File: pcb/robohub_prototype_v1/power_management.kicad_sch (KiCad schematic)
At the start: 134 parts, among them J21 Barrel_Jack_Switch_Pin3Ring, U21 LM3880, U22 TPS564242DRL, U23 TPS564242DRL, U24 TPS564242DRL, U25 TPS564242DRL, U26 TPS564242DRL, U27 TPS564242DRL

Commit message: Update paths to footprint libraries. Begin adding footprints for PDN resistors. Create master BOM
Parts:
- R211, R216, R217, R220, R224, R27, R28: footprint (none) -> Resistor_SMD:R_0402_1005Metric
- U22, U23, U24, U25, U26, U27: footprint custom_footprint:TPS564247DRLR -> fryelabs:TPS564247DRLR
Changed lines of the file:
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@@
 			)
 		)
-		(property "Footprint" "custom_footprint:TPS564247DRLR"
+		(property "Footprint" "fryelabs:TPS564247DRLR"
 			(at 165.1 134.62 0)
 			(effects
@@
 			)
 		)
-		(property "Footprint" "custom_footprint:TPS564247DRLR"
+		(property "Footprint" "fryelabs:TPS564247DRLR"
 			(at 163.83 257.81 0)
 			(effects
@@
 			)
 		)
-		(property "Footprint" ""
+		(property "Footprint" "Resistor_SMD:R_0402_1005Metric"
 			(at 130.302 262.89 90)
 			(effects
@@
 			)
 		)
-		(property "Footprint" "custom_footprint:TPS564247DRLR"
+		(property "Footprint" "fryelabs:TPS564247DRLR"
 			(at 162.56 381 0)
 			(effects
@@
 			)
 		)
-		(property "Footprint" ""
+		(property "Footprint" "Resistor_SMD:R_0402_1005Metric"
 			(at 130.302 325.12 90)
 			(effects
@@
 			)
 		)
-		(property "Footprint" ""
+		(property "Footprint" "Resistor_SMD:R_0402_1005Metric"
 			(at 187.452 320.04 90)
 			(effects
@@
 			)
 		)
-		(property "Footprint" ""
+		(property "Footprint" "Resistor_SMD:R_0402_1005Metric"
 			(at 129.032 445.77 90)
 			(effects
@@
 			)
 		)
-		(property "Footprint" ""
+		(property "Footprint" "Resistor_SMD:R_0402_1005Metric"
 			(at 187.452 198.12 90)
 			(effects
@@
 			)
 		)
-		(property "Footprint" ""
+		(property "Footprint" "Resistor_SMD:R_0402_1005Metric"
 			(at 129.032 386.08 90)
 			(effects
@@
 			)
 		)
-		(property "Footprint" "custom_footprint:TPS564247DRLR"
+		(property "Footprint" "fryelabs:TPS564247DRLR"
 			(at 163.83 198.12 0)
 			(effects
@@
 			)
 		)
-		(property "Footprint" ""
+		(property "Footprint" "Resistor_SMD:R_0402_1005Metric"
 			(at 130.302 203.2 90)
 			(effects
@@
 			)
 		)
-		(property "Footprint" "custom_footprint:TPS564247DRLR"
+		(property "Footprint" "fryelabs:TPS564247DRLR"
 			(at 162.56 440.69 0)
 			(effects
@@
 			)
 		)
-		(property "Footprint" "custom_footprint:TPS564247DRLR"
+		(property "Footprint" "fryelabs:TPS564247DRLR"
 			(at 163.83 320.04 0)
 			(effects

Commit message: Begin PDN circuit design/BOM/layout
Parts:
- removed D21, D22, D23: D_Schottky, symbol Device:D_Schottky
- C210, C217, C218, C228, C229, C29: footprint (none) -> Capacitor_SMD:C_0603_1608Metric
- C214, C215, C216, C226, C227, C26, C2602, C27, C28: footprint (none) -> Capacitor_SMD:C_1206_3216Metric
- L21, L24, L25: value 1u -> 2.2u; footprint (none) -> Inductor_SMD:L_0805_2012Metric
- R21, R210, R215, R219, R223, R26: footprint (none) -> Resistor_SMD:R_0402_1005Metric
- R212, R23: value 135k -> 100k; footprint (none) -> Resistor_SMD:R_0402_1005Metric
- R213, R24, R29: value 30k -> 22.1k; footprint (none) -> Resistor_SMD:R_0402_1005Metric
- R22: footprint (none) -> Resistor_SMD:R_0603_1608Metric
- R28: value 135k -> 100k
- U22, U23, U24, U25, U26, U27: footprint fryelabs:TPS564247DRLR -> fryelabs_kicad_footprint_lib:TPS564247DRLR
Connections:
- net VCC_3_3_A_SW: now reaches L21.1, U22.2 (SW)
- net VCC_3A_EN: now reaches R21.2, R22.1, U22.5 (EN)
- net VCC_3_3_A_FB: now reaches R23.2, R24.1, U22.6 (FB)
- net VCC_3_3_C_SW: now reaches L25.1, U24.2 (SW)
- net VCC_3_3C_EN: now reaches R210.2, R211.1, U24.5 (EN)
- net VCC_3_3_C_FB: now reaches R212.2, R213.1, U24.6 (FB)
- net VCC_3_3_B_FB: now reaches R28.2, R29.1, U23.6 (FB)
- net VCC_3_3B_EN: now reaches R26.2, R27.1, U23.5 (EN)
- net VCC_3_3_B_SW: now reaches L24.1, U23.2 (SW)
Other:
- note added: "- Processor Clock Frequency 500MHz"
- note added: "Key: R1 = R23 R2 = R24"
- note added: "Relevant Info for PDN"
- note added: "V_out = 0.6*(1+(R1/R2))"
- moved on the sheet: C210, C214, C215, C216, C226, C227, C26, C2602, C27, C28, C29, R21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

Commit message: Update paths for footprints top adjacent lib directory at above clone. Finish basic regulator layout/BOM. Link 3d STEPs into model. Rearrangle layout
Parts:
- removed D24, D25, D26: D_Schottky, symbol Device:D_Schottky
- removed R210, R219, R223, R26: 100k, Resistor_SMD:R_0402_1005Metric, symbol Device:R
- removed R211, R220, R224, R27: 36.5k, Resistor_SMD:R_0402_1005Metric, symbol Device:R
- C233, C234, C235, C240, C241, C242, C257, C258, C259: footprint (none) -> Capacitor_SMD:C_1206_3216Metric
- C236, C237, C243, C244, C260, C261: footprint (none) -> Capacitor_SMD:C_0603_1608Metric
- L26, L28, L29: footprint (none) -> Inductor_SMD:L_0805_2012Metric
- R216: footprint Resistor_SMD:R_0402_1005Metric -> Resistor_SMD:R_0603_1608Metric
- R218, R221, R222: footprint (none) -> Resistor_SMD:R_0402_1005Metric
- R225: value 95k -> 32k; footprint (none) -> Resistor_SMD:R_0402_1005Metric
- R226: value 30k -> 10k; footprint (none) -> Resistor_SMD:R_0402_1005Metric
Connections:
- net VCC_3A_EN is gone; now on net PS_GRP1_EN_DIV: R21.2, R22.1, U22.5 (EN)
- net VCC_3_3B_EN is gone; now on net PS_GRP1_EN_DIV: U23.5 (EN)
- net VCC_3_3C_EN is gone; now on net PS_GRP1_EN_DIV: U24.5 (EN)
- net VCC_1_2_DDR_SW: now reaches L28.1, U26.2 (SW)
- net PS_GRP1_EN_DIV: now reaches U26.5 (EN)
- net VCC_1_2_DDR_FB: now reaches R221.2, R222.1, U26.6 (FB)
- net PS_GRP2_EN_DIV: now reaches R215.2, R216.1, U25.5 (EN)
- net PS_GRP2_EN_DIV: now also U27.5 (EN)
- net VCC_1_2_FB: now reaches R217.2, R218.1, U25.6 (FB)
- net VCC_1_2_SW: now reaches L26.1, U25.2 (SW)
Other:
- moved on the sheet: C233, C234, C235, C240, C241, C242, C257, C258, C259, R215, R216, U25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

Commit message: Add fuse to PCB design
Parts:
- added F1: Fuse, fryelabs_kicad_footprint_lib:0ZCF0050FF2C, symbol Device:Fuse
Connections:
- net 5V: now also F1.2; no longer J21.1
- new net VCC: F1.1, J21.1
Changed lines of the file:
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@@
 	)
 	(junction
+		(at 67.31 73.66)
+		(diameter 0)
+		(color 0 0 0 0)
+	)
+	(junction
 		(at 353.06 412.75)
 		(diameter 0)
@@
 	(polyline
 		(pts
-			(xy 83.82 91.44) (xy 83.82 48.26)
+			(xy 105.41 92.71) (xy 105.41 49.53)
 		)
 		(stroke
@@
 		)
 	)
-	(polyline
-		(pts
-			(xy 25.4 48.26) (xy 25.4 50.8)
-		)
-		(stroke
-			(width 0)
-			(type default)
-		)
-	)
 	(wire
 		(pts
@@
 	(wire
 		(pts
+			(xy 67.31 73.66) (xy 72.39 73.66)
+		)
+		(stroke
+			(width 0)
+			(type default)
+		)
+	)
+	(wire
+		(pts
 			(xy 316.23 412.75) (xy 316.23 426.72)
 		)
@@
 	(polyline
 		(pts
-			(xy 25.4 91.44) (xy 83.82 91.44)
+			(xy 25.4 92.71) (xy 105.41 92.71)
 		)
 		(stroke
@@
 	(polyline
 		(pts
-			(xy 25.4 52.07) (xy 25.4 91.44)
+			(xy 25.4 49.53) (xy 25.4 91.44)
 		)
 		(stroke
@@
 	(wire
 		(pts
+			(xy 86.36 67.31) (xy 86.36 73.66)
+		)
+		(stroke
+			(width 0)
+			(type default)
+		)
+	)
+	(wire
+		(pts
 			(xy 111.76 314.96) (xy 111.76 317.5)
 		)
@@
 	(polyline
 		(pts
-			(xy 83.82 48.26) (xy 25.4 48.26)
+			(xy 105.41 49.53) (xy 25.4 49.53)
 		)
 		(stroke
@@
 	(wire
 		(pts
+			(xy 80.01 73.66) (xy 86.36 73.66)
+		)
+		(stroke
+			(width 0)
+			(type default)
+		)
+	)
+	(wire
+		(pts
 			(xy 210.82 199.39) (xy 210.82 193.04)
 		)
@@
 	(global_label "5V"
 		(shape input)
+		(at 86.36 67.31 90)
+		(fields_autoplaced yes)
+		(effects
+			(font
+				(size 1.27 1.27)
+			)
+			(justify left)
+		)
+		(property "Intersheetrefs" "${INTERSHEET_REFS}"
+			(at 86.2806 62.5988 90)
+			(effects
+				(font
+					(size 1.27 1.27)
+				)
+				(justify left)
+				(hide yes)
+			)
+		)
+	)
+	(global_label "VCC"
+		(shape input)
 		(at 67.31 67.31 90)
 		(fields_autoplaced yes)
@@
 		)
 		(property "Intersheetrefs" "${INTERSHEET_REFS}"
-			(at 67.2306 62.5988 90)
+			(at 67.31 60.6962 90)
 			(effects
 				(font
@@
 					(unit 1)
 				)
+			)
+		)
+	)
+	(symbol
+		(lib_id "Device:Fuse")
+		(at 76.2 73.66 90)
+		(unit 1)
+		(exclude_from_sim no)
+		(in_bom yes)
+		(on_board yes)
+		(dnp no)
+		(fields_autoplaced yes)
+		(property "Reference" "F1"
+			(at 76.2 67.31 90)
+			(effects
+				(font
+					(size 1.27 1.27)
+				)
+			)
+		)
+		(property "Value" "Fuse"
+			(at 76.2 69.85 90)
+			(effects
+				(font
+					(size 1.27 1.27)
+				)
+			)
+		)
+		(property "Footprint" "fryelabs_kicad_footprint_lib:0ZCF0050FF2C"
+			(at 76.2 75.438 90)
+			(effects
+				(font
+					(size 1.27 1.27)
+				)
+				(hide yes)
+			)
+		)
+		(property "Datasheet" "~"
+			(at 76.2 73.66 0)
+			(effects
+				(font
+					(size 1.27 1.27)
+				)
+				(hide yes)
+			)
+		)
+		(property "Description" "Fuse"
+			(at 76.2 73.66 0)
+			(effects
+				(font
+					(size 1.27 1.27)
+				)
+				(hide yes)
+			)
+		)
+		(pin "2"
+		)
+		(pin "1"
+		)
+		(instances
+			(project "robohub_prototype_v1"
+				(path "/bc29dce2-fa63-43eb-9ef7-3b495f27cc69/73c1b947-11e9-40cf-af03-56c22766304e"
+					(reference "F1")
+					(unit 1)
+				)

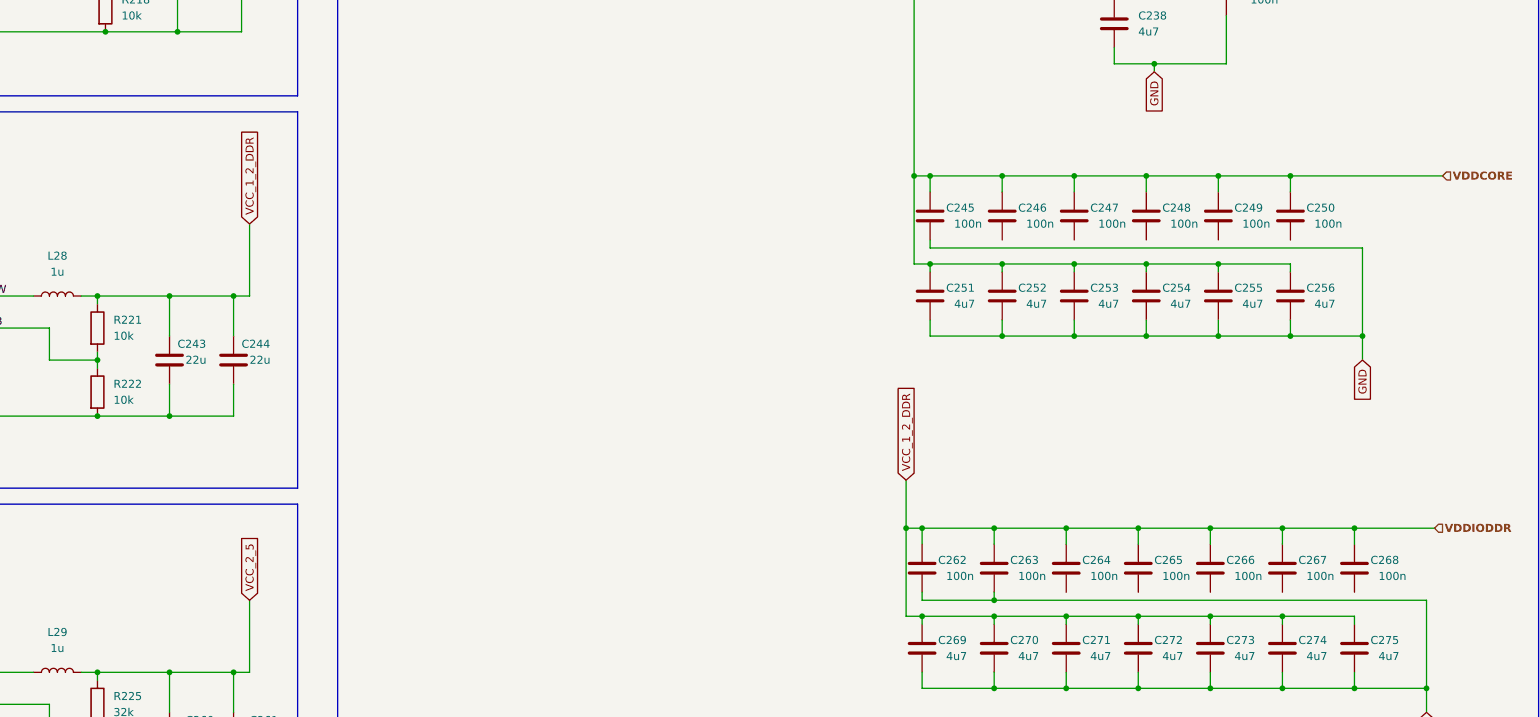
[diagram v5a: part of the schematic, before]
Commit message: Update schematic and pcb with net groups for routing DDR2
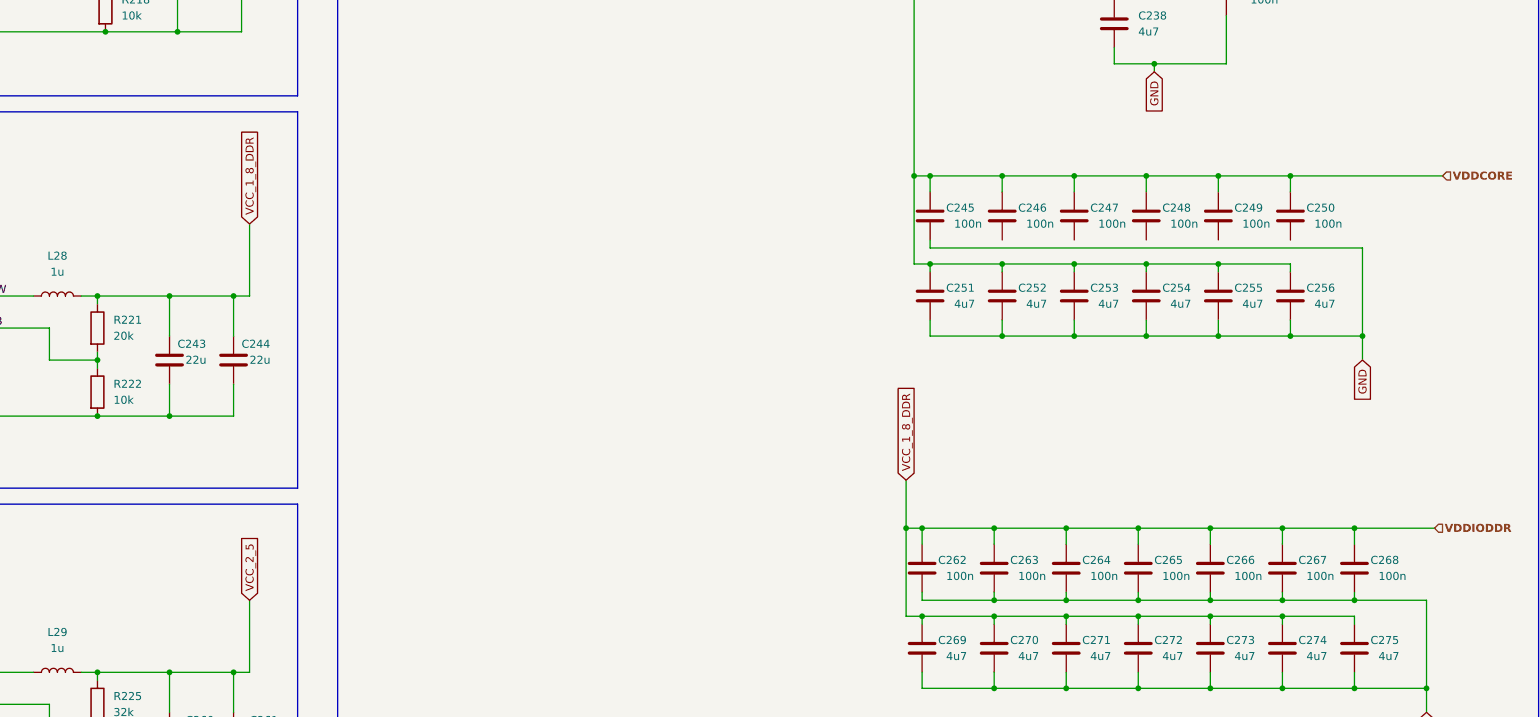
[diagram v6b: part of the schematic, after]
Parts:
- R221: value 10k -> 20k
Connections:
- net GND: now also C264.2, C265.2, C266.2, C267.2, C268.2
- net VCC_1_2_DDR: no longer C243.1, C244.1, C262.1, C263.1, C264.1, C265.1, C266.1, C267.1, C268.1, C269.1, C270.1, C271.1, C272.1, C273.1, C274.1, C275.1, L28.2, R221.1
- new net VCC_1_8_DDR: C243.1, C244.1, C262.1, C263.1, C264.1, C265.1, C266.1, C267.1, C268.1, C269.1, C270.1, C271.1, C272.1, C273.1, C274.1, C275.1, L28.2, R221.1
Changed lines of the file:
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@@
 	(paper "C" portrait)
 	(junction
+		(at 364.49 424.18)
+		(diameter 0)
+		(color 0 0 0 0)
+	)
+	(junction
 		(at 353.06 426.72)
 		(diameter 0)
@@
 	)
 	(junction
+		(at 375.92 424.18)
+		(diameter 0)
+		(color 0 0 0 0)
+	)
+	(junction
 		(at 367.03 289.56)
 		(diameter 0)
@@
 	)
 	(junction
+		(at 353.06 424.18)
+		(diameter 0)
+		(color 0 0 0 0)
+	)
+	(junction
 		(at 104.14 113.03)
 		(diameter 0)
@@
 	)
 	(junction
+		(at 341.63 424.18)
+		(diameter 0)
+		(color 0 0 0 0)
+	)
+	(junction
 		(at 187.96 445.77)
 		(diameter 0)
@@
 	)
 	(junction
+		(at 387.35 424.18)
+		(diameter 0)
+		(color 0 0 0 0)
+	)
+	(junction
 		(at 250.19 83.82)
 		(diameter 0)
@@
 	(wire
 		(pts
+			(xy 387.35 424.18) (xy 398.78 424.18)
+		)
+		(stroke
+			(width 0)
+			(type default)
+		)
+	)
+	(wire
+		(pts
 			(xy 199.39 449.58) (xy 199.39 454.66)
 		)
@@
 		)
 	)
+	(wire
+		(pts
+			(xy 341.63 424.18) (xy 353.06 424.18)
+		)
+		(stroke
+			(width 0)
+			(type default)
+		)
+	)
 	(polyline
 		(pts
@@
 	(wire
 		(pts
+			(xy 375.92 424.18) (xy 387.35 424.18)
+		)
+		(stroke
+			(width 0)
+			(type default)
+		)
+	)
+	(wire
+		(pts
 			(xy 78.74 393.7) (xy 88.9 393.7)
 		)
@@
 	(wire
 		(pts
+			(xy 364.49 422.91) (xy 364.49 424.18)
+		)
+		(stroke
+			(width 0)
+			(type default)
+		)
+	)
+	(wire
+		(pts
 			(xy 204.47 143.51) (xy 204.47 148.59)
 		)
@@
 	(wire
 		(pts
+			(xy 375.92 422.91) (xy 375.92 424.18)
+		)
+		(stroke
+			(width 0)
+			(type default)
+		)
+	)
+	(wire
+		(pts
 			(xy 320.04 356.87) (xy 320.04 359.41)
 		)
@@
 	(wire
 		(pts
+			(xy 353.06 422.91) (xy 353.06 424.18)
+		)
+		(stroke
+			(width 0)
+			(type default)
+		)
+	)
+	(wire
+		(pts
 			(xy 250.19 86.36) (xy 250.19 83.82)
 		)
@@
 	(wire
 		(pts
-			(xy 330.2 424.18) (xy 398.78 424.18)
+			(xy 330.2 424.18) (xy 341.63 424.18)
 		)
 		(stroke
@@
 	(wire
 		(pts
+			(xy 353.06 424.18) (xy 364.49 424.18)
+		)
+		(stroke
+			(width 0)
+			(type default)
+		)
+	)
+	(wire
+		(pts
 			(xy 200.66 314.96) (xy 189.23 314.96)
 		)
@@
 		)
 	)
+	(wire
+		(pts
+			(xy 364.49 424.18) (xy 375.92 424.18)
+		)
+		(stroke
+			(width 0)
+			(type default)
+		)
+	)
 	(polyline
 		(pts
@@
 	(wire
 		(pts
+			(xy 387.35 422.91) (xy 387.35 424.18)
+		)
+		(stroke
+			(width 0)
+			(type default)
+		)
+	)
+	(wire
+		(pts
 			(xy 92.71 419.1) (xy 102.87 419.1)
 		)
@@
 	(wire
 		(pts
+			(xy 341.63 422.91) (xy 341.63 424.18)
+		)
+		(stroke
+			(width 0)
+			(type default)
+		)
+	)
+	(wire
+		(pts
 			(xy 354.33 300.99) (xy 354.33 302.26)
 		)
@@
 		)
 	)
-	(global_label "VCC_1_2_DDR"
+	(global_label "VCC_1_8_DDR"
 		(shape input)
 		(at 316.23 405.13 90)
@@
 		)
 		(property "Intersheetrefs" "${INTERSHEET_REFS}"
-			(at 316.1506 389.9564 90)
+			(at 316.23 389.3844 90)
 			(effects
 				(font
@@
 		)
 	)
-	(global_label "VCC_1_2_DDR"
+	(global_label "VCC_1_8_DDR"
 		(shape input)
 		(at 212.09 364.49 90)
@@
 		)
 		(property "Intersheetrefs" "${INTERSHEET_REFS}"
-			(at 212.0106 349.3164 90)
+			(at 212.09 348.7444 90)
 			(effects
 				(font
@@
 			)
 		)
-		(property "Value" "10k"
+		(property "Value" "20k"
 			(at 190.5 382.2699 0)
 			(effects
